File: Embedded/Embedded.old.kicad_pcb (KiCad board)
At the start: 2 copper layers, 77.5 x 106.5 mm, 102 parts, among them J1 GyroBreakout, J2 Conn_01x08, J3 Conn_01x08, J6 Conn_01x08, J7 Conn_01x08, M1 Fan, Q1 FQP27P06, SW1 BackboardSw, U1 ESP32-C6-WROOM-1, U2 BQ25895RTW, U3 FSUSB30MUX, U5 MP8715, U7 SN74AHCT125N, U8 SN74AHCT125N

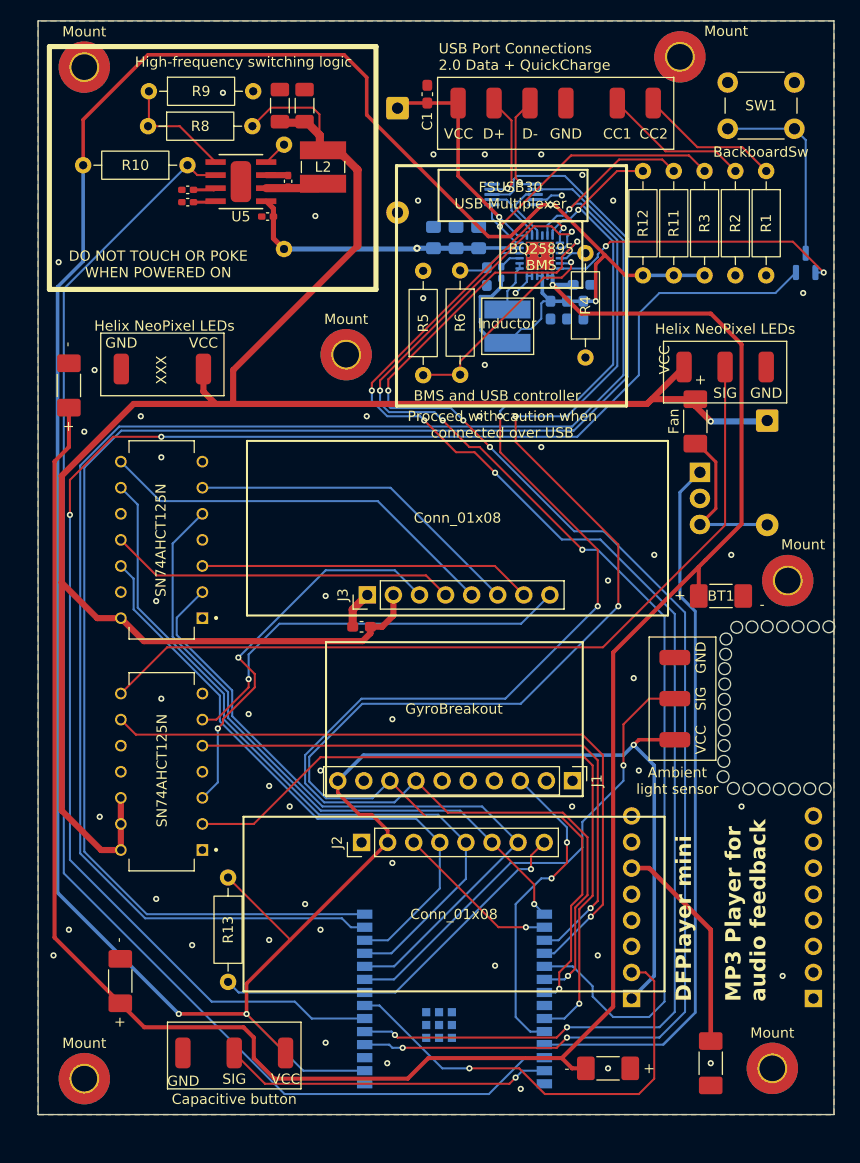
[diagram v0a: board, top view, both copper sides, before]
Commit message: Overhaul
Redesign, Ground for UWP/Droid app, Switch from Arduino C to ESP-IDF with native C
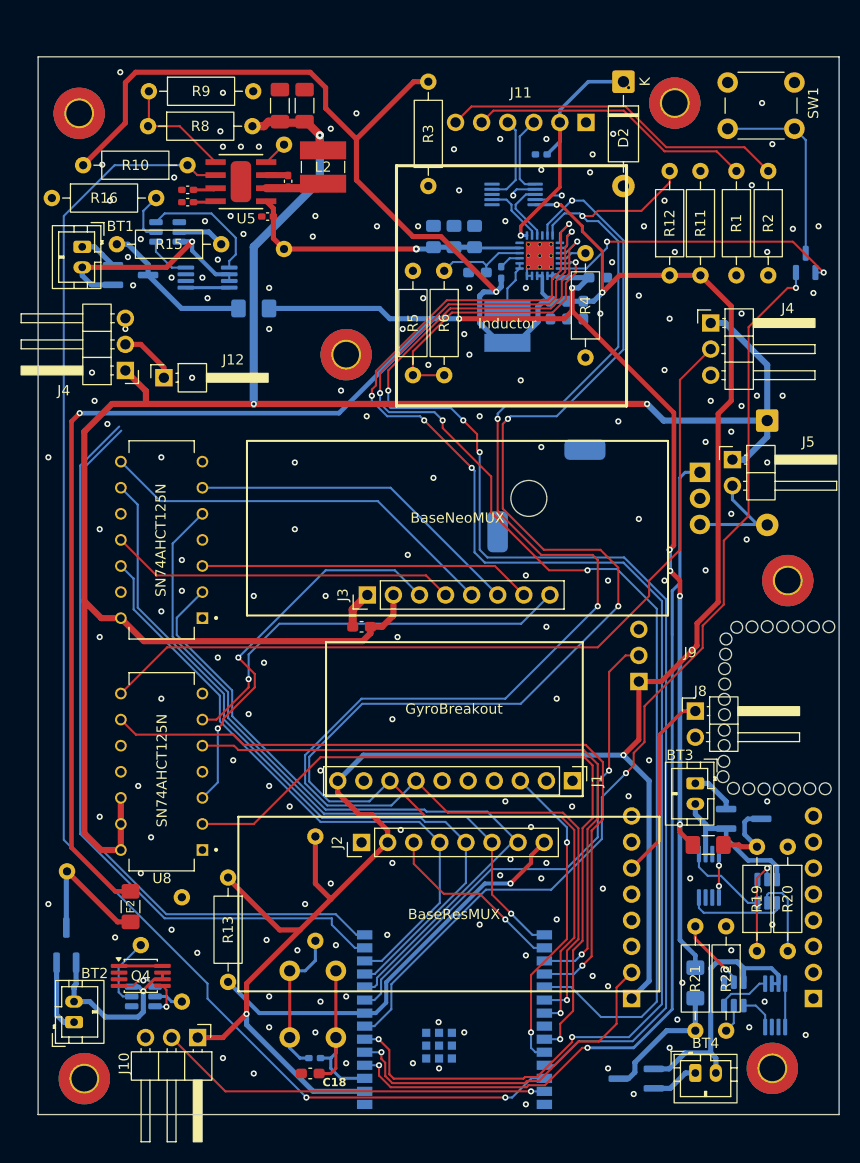
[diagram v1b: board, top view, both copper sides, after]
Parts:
- removed ALS1, H9, Neo3 (x2), Touch3: GND, Connector_Wire:SolderWirePad_1x01_SMD_1.5x3mm
- removed ALS2, Neo2, Touch2: SIG, Connector_Wire:SolderWirePad_1x01_SMD_1.5x3mm
- removed ALS3, H12, Neo1 (x2), Touch1: VCC, Connector_Wire:SolderWirePad_1x01_SMD_1.5x3mm
- removed the BT2 at (165.0, 138.5)
- removed the BT2 at (112.5, 72.0)
- removed the BT2 at (117.5, 130.0)
- removed H10: CC1, Connector_Wire:SolderWirePad_1x01_SMD_1.5x3mm
- removed H11: CC2, Connector_Wire:SolderWirePad_1x01_SMD_1.5x3mm
- removed H7: D-, Connector_Wire:SolderWirePad_1x01_SMD_1.5x3mm
- removed H8: D+, Connector_Wire:SolderWirePad_1x01_SMD_1.5x3mm
- removed LS1: Speaker, Capacitor_SMD:C_1808_4520Metric_Pad1.72x2.30mm_HandSolder
- removed M1: Fan, Capacitor_SMD:C_1808_4520Metric_Pad1.72x2.30mm_HandSolder
- added ?: , , B.Cu at (154.2, 86.2)
- added ?: , , F.Cu at (162.8, 78.2)
- added BT2: Battery_Cell, Connector_JST:JST_PH_B2B-PH-K_1x02_P2.00mm_Vertical, F.Cu at (113.0, 134.0)
- added BT3: Battery_Cell, Connector_JST:JST_PH_B2B-PH-K_1x02_P2.00mm_Vertical, F.Cu at (173.5, 110.8)
- added BT4: Battery_Cell, Connector_JST:JST_PH_B2B-PH-K_1x02_P2.00mm_Vertical, F.Cu at (173.5, 138.9)
- added C17: 100nF, Capacitor_SMD:C_0402_1005Metric_Pad0.74x0.62mm_HandSolder, B.Cu at (136.4, 137.5)
- added C18: 1uF, Capacitor_SMD:C_0603_1608Metric_Pad1.08x0.95mm_HandSolder, F.Cu at (136.0, 139.0)
- added F1: Polyfuse, Fuse:Fuse_1206_3216Metric_Pad1.42x1.75mm_HandSolder, B.Cu at (130.5, 64.5)
- added F2: Polyfuse, Fuse:Fuse_1206_3216Metric_Pad1.42x1.75mm_HandSolder, F.Cu at (118.5, 122.8)
- added F3: Polyfuse, Fuse:Fuse_1206_3216Metric_Pad1.42x1.75mm_HandSolder, F.Cu at (174.8, 116.8)
- added F4: Polyfuse, Fuse:Fuse_1206_3216Metric_Pad1.42x1.75mm_HandSolder, B.Cu at (173.5, 130.2)
- added J10: TouchButton, Connector_PinHeader_2.54mm:PinHeader_1x03_P2.54mm_Horizontal, F.Cu at (125.0, 135.5)
- added J11: USB-C Breakout, Connector_PinHeader_2.54mm:PinHeader_1x06_P2.54mm_Horizontal, B.Cu at (162.8, 46.4)
- added J12: HelixNeoSig-Cont, Connector_PinHeader_2.54mm:PinHeader_1x01_P2.54mm_Horizontal, F.Cu at (121.8, 71.2)
- added J4: HelixNeo, Connector_PinHeader_2.54mm:PinHeader_1x03_P2.54mm_Horizontal, F.Cu at (118.0, 70.5)
- added J4: HelixNeo, Connector_PinHeader_2.54mm:PinHeader_1x03_P2.54mm_Horizontal, F.Cu at (175.0, 65.9)
- added J5: FanConnector, Connector_PinHeader_2.54mm:PinHeader_1x02_P2.54mm_Horizontal, F.Cu at (177.1, 79.2)
- added J8: Speaker, Connector_PinHeader_2.54mm:PinHeader_1x02_P2.54mm_Horizontal, F.Cu at (173.5, 103.7)
- added J9: LightSensor, Connector_PinHeader_2.54mm:PinHeader_1x03_P2.54mm_Horizontal, B.Cu at (168.0, 100.8)
- added Q2: FS8205A, Package_SO:MSOP-8_3x3mm_P0.65mm, B.Cu at (126.0, 61.5)
- added Q3: AO3401A, Package_TO_SOT_SMD:TSOT-23_HandSoldering, B.Cu at (118.5, 61.2)
- added Q4: FS8205A, Package_SO:MSOP-8_3x3mm_P0.65mm, F.Cu at (119.5, 129.5)
- added Q5: AO3401A, Package_TO_SOT_SMD:TSOT-23_HandSoldering, B.Cu at (112.2, 126.5)
- added Q6: FS8205A, Package_SO:MSOP-8_3x3mm_P0.65mm, B.Cu at (174.8, 119.8)
- added Q7: AO3401A, Package_TO_SOT_SMD:TSOT-23_HandSoldering, B.Cu at (178.2, 114.2)
- added Q8: FS8205A, Package_SO:MSOP-8_3x3mm_P0.65mm, B.Cu at (181.3, 132.4)
- added Q9: AO3401A, Package_TO_SOT_SMD:TSOT-23_HandSoldering, B.Cu at (167.8, 139.5)
- added R14: 10k, Resistor_THT:R_Axial_DIN0207_L6.3mm_D2.5mm_P10.16mm_Horizontal, B.Cu at (136.5, 126.1)
- added R15: 100, Resistor_THT:R_Axial_DIN0207_L6.3mm_D2.5mm_P10.16mm_Horizontal, F.Cu at (127.3, 58.2)
- added R16: 100, Resistor_THT:R_Axial_DIN0207_L6.3mm_D2.5mm_P10.16mm_Horizontal, F.Cu at (110.8, 53.8)
- added R17: 100, Resistor_THT:R_Axial_DIN0207_L6.3mm_D2.5mm_P10.16mm_Horizontal, B.Cu at (119.5, 126.5)
- added R18: 100, Resistor_THT:R_Axial_DIN0207_L6.3mm_D2.5mm_P10.16mm_Horizontal, B.Cu at (123.5, 121.8)
- added R19: 100, Resistor_THT:R_Axial_DIN0207_L6.3mm_D2.5mm_P10.16mm_Horizontal, F.Cu at (179.5, 127.1)
- added R20: 100, Resistor_THT:R_Axial_DIN0207_L6.3mm_D2.5mm_P10.16mm_Horizontal, F.Cu at (182.5, 116.9)
- added R21: 100, Resistor_THT:R_Axial_DIN0207_L6.3mm_D2.5mm_P10.16mm_Horizontal, F.Cu at (173.5, 124.7)
- added R22: 100, Resistor_THT:R_Axial_DIN0207_L6.3mm_D2.5mm_P10.16mm_Horizontal, F.Cu at (176.5, 124.7)
- added SW2: BackboardSw, Button_Switch_THT:SW_PUSH_6mm_H5mm, B.Cu at (138.5, 135.5)
- added U10: DW01A, Package_TO_SOT_SMD:SOT-23-6, B.Cu at (177.2, 131.2)
- added U4: DW01A, Package_TO_SOT_SMD:SOT-23-6, B.Cu at (122.1, 57.0)
- added U6: DW01A, Package_TO_SOT_SMD:SOT-23-6, B.Cu at (119.8, 131.5)
- added U9: DW01A, Package_TO_SOT_SMD:SOT-23-6, B.Cu at (180.5, 121.2)
- BT1: footprint Capacitor_SMD:C_1808_4520Metric_Pad1.72x2.30mm_HandSolder -> Connector_JST:JST_PH_B2B-PH-K_1x02_P2.00mm_Vertical
- C1: footprint Capacitor_SMD:C_0603_1608Metric_Pad1.08x0.95mm_HandSolder -> Capacitor_SMD:C_0402_1005Metric_Pad0.74x0.62mm_HandSolder; moved to B.Cu
- C13: value 10nF -> 100nF
- D2: moved to F.Cu
- J2: value Conn_01x08 -> BaseResMUX
- J3: value Conn_01x08 -> BaseNeoMUX
- Q1: footprint Package_TO_SOT_THT:TO-220-3_Vertical -> Package_TO_SOT_THT:TO-220-3_Horizontal_TabDown
- R13: value 4.7k -> 10k
- moved BT1 70.9 mm to (113.8, 58.5), turned to -90 degrees
- moved R3 26.9 mm to (147.5, 52.6), turned to 90 degrees
- moved D2 22.2 mm to (166.5, 42.4)
- moved C1 12.6 mm to (158.5, 49.5), turned to 180 degrees
- moved Mount 4.53 mm to (113.5, 45.5)
- moved Mount 4.53 mm to (171.5, 44.5)
- moved R2 3.20 mm to (180.6, 51.1)
- moved R1 2.90 mm to (177.5, 51.1)
- moved R11 2.60 mm to (174.0, 61.3)
- moved R12 2.60 mm to (171.0, 61.3)
- moved U1 2.01 mm to (150.1, 133.8)
- moved C8 1.69 mm to (164.0, 61.5), turned to 180 degrees
- moved R6 1.56 mm to (149.0, 60.8)
- moved R5 1.00 mm to (146.0, 71.0)
- moved C9 1.00 mm to (152.3, 61.0), turned to 0 degrees
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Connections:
- net Net-(D1-A) renamed /FanOut
- net Net-(D2-K) renamed /UsbVBUS
- net Net-(J1-Pin_3) renamed /GyroInt
- net Net-(J1-Pin_7) renamed /SDA
- net Net-(J1-Pin_8) renamed /SCL
- net Net-(J2-Pin_3) renamed /BaseResEN
- net Net-(J2-Pin_4) renamed /MuxS0
- net Net-(J2-Pin_5) renamed /MuxS1
- net Net-(J2-Pin_6) renamed /MuxS2
- net Net-(J2-Pin_7) renamed /MuxS3
- net Net-(J2-Pin_8) renamed /BaseResSIG
- net Net-(J3-Pin_4) renamed /BaseNeoS0
- net Net-(J3-Pin_5) renamed /BaseNeoS1
- net Net-(J3-Pin_6) renamed /BaseNeoS2
- net Net-(J3-Pin_7) renamed /BaseNeoS3
- net Net-(U1-GPIO12/USB_D-) renamed /EspD-
- net Net-(U1-GPIO13/USB_D+) renamed /EspD+
- net Net-(U1-GPIO15) renamed /BaseNeoEN
- net Net-(U1-GPIO19) renamed /BaseNeoSIG
- net Net-(U1-GPIO20) renamed /HelixNeoSIG
- net Net-(U1-GPIO21) renamed /BmsOTG
- net Net-(U1-GPIO3/ADC1_CH3) renamed /BuckPOK
- net Net-(U2-DSEL) renamed /UsbDSEL
- net Net-(U2-~{QON}) renamed /BackboardIcBtn
- BT1 pad 2: GND -> Net-(BT1--)
- C8 pad 1: Net-(BT1-+) -> GND
- C8 pad 2: GND -> BATT
- D3 pad 2: Net-(U1-MTCK/GPIO6/ADC1_CH6) -> /BackboardBtn
- J6 pad 2: Net-(J6-Pin_2) -> /DFPlayer
- J6 pad 6: Net-(J6-Pin_6) -> /Spk+
- Q1 pad 1: Net-(Q1-G) -> /FanControl
- U1 pad 25: Net-(Q1-G) -> /BmsCE
- U1 pad 27: Net-(U1-GPIO2/ADC1_CH2) -> /TouchBtn
- U1 pad 3: unconnected-(U1-EN/CHIP_PU-Pad3) -> Net-(U1-EN/CHIP_PU)
- U1 pad 4: Net-(U1-MTMS/GPIO4/ADC1_CH4) -> /FanControl
- U1 pad 5: Net-(U1-MTDI/GPIO5/ADC1_CH5) -> /DFPlayer
- U1 pad 6: Net-(U1-MTCK/GPIO6/ADC1_CH6) -> /BmsInt
- U1 pad 7: Net-(J6-Pin_2) -> /BackboardBtn
- U1 pad 9: Net-(U1-GPIO1/ADC1_CH1/XTAL_32K_N) -> /ALS
- U2 pad 13: Net-(BT1-+) -> BATT
- U2 pad 14: Net-(BT1-+) -> BATT
- U2 pad 7: Net-(U1-MTDI/GPIO5/ADC1_CH5) -> /BmsInt
- U2 pad 9: Net-(U1-MTMS/GPIO4/ADC1_CH4) -> /BmsCE
- U3 pad 4: Net-(U3-D+) -> /UsbD+
- U3 pad 6: Net-(U3-D-) -> /UsbD-
- U8 pad 8: Net-(U8-3Y) -> /HelixNeo
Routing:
- net Net-(BT1-+): track 215.8 -> 3.74 mm, vias 1 -> 0
- net BATT: track 0.00 -> 198.8 mm, vias 0 -> 7
- net Net-(U1-MTCK/GPIO6/ADC1_CH6): track 154.7 -> 0.00 mm, vias 2 -> 0
- net /BmsInt: track 0.00 -> 148.6 mm, vias 0 -> 6
- net Net-(U1-MTMS/GPIO4/ADC1_CH4): track 138.2 -> 0.00 mm, vias 6 -> 0
- net Net-(U1-MTDI/GPIO5/ADC1_CH5): track 137.1 -> 0.00 mm, vias 6 -> 0
- net /BmsCE: track 0.00 -> 126.7 mm, vias 0 -> 4
- net /BackboardBtn: track 0.00 -> 95.5 mm, vias 0 -> 2
- net /FanControl: track 0.00 -> 88.8 mm, vias 0 -> 2
- net /EspD+: track 154.4 -> 72.0 mm
- net /HelixNeo: track 0.00 -> 81.9 mm
- net Net-(U8-3Y): track 81.0 -> 0.00 mm
- net /EspD-: track 148.8 -> 76.4 mm, vias 0 -> 1
- net Net-(Q1-G): track 70.0 -> 0.00 mm
- net /ALS: track 0.00 -> 50.2 mm, vias 0 -> 1
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- removed copper zone on B.Cu, net GND
- removed copper zone on F.Cu, net GND
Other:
- board size 77.5 x 106.5 mm -> 78 x 103 mm
- board text removed: "+"
- board text removed: "-"
- board text removed: "Ambient light sensor"
- board text removed: "BMS and USB controller"
- board text removed: "BQ25895 BMS"
- board text removed: "Capacitive button"
- board text removed: "DFPlayer mini MP3 Player for audio feedback"
- board text removed: "DO NOT TOUCH OR POKE WHEN POWERED ON"
- board text removed: "FSUSB30 USB Multiplexer"
- board text removed: "Helix NeoPixel LEDs"
- board text removed: "High-frequency switching logic"
- board text removed: "Procced with caution when connected over USB"
- board text removed: "USB Port Connections 2.0 Data + QuickCharge"
- board text removed: "XXX"
